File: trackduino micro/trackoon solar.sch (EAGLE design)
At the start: 53 parts, among them IC1 MCP73871, IC2 74AHC1G125DBV, SW1 SPST_TACT-KMR2, U1 ATMEGA168MLF, Y1 16MHZ

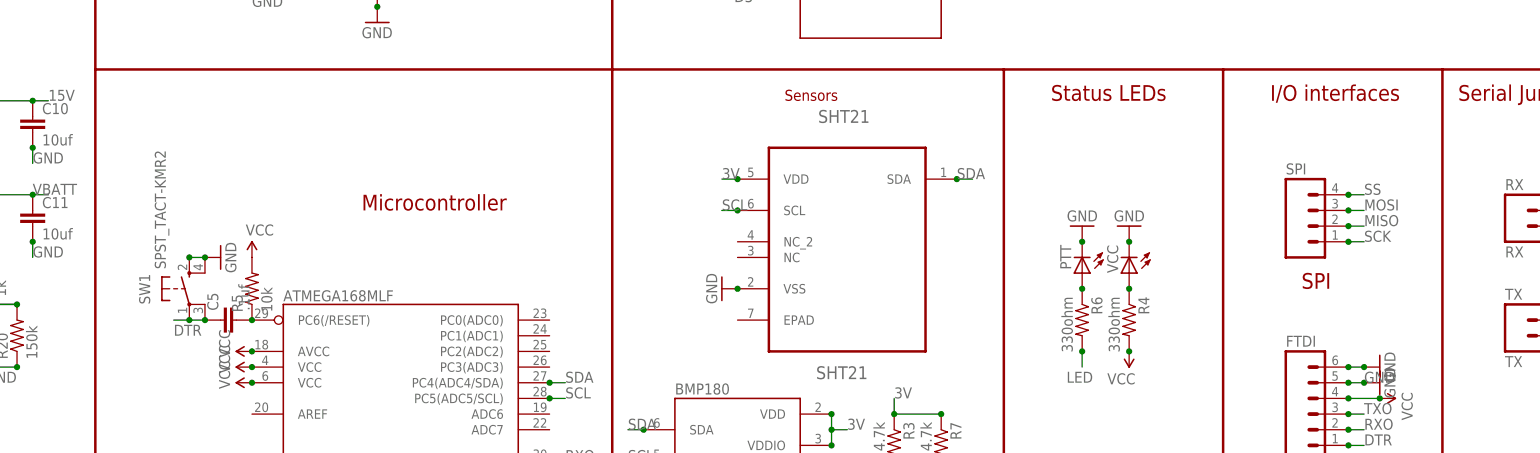
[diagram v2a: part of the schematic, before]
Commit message: added i2c breakout and fixed ftdi
added breakouts on all versions for i2c next to the spi header, replaced
IO breakout headers from .1" to 2mm to accomodate i2c.
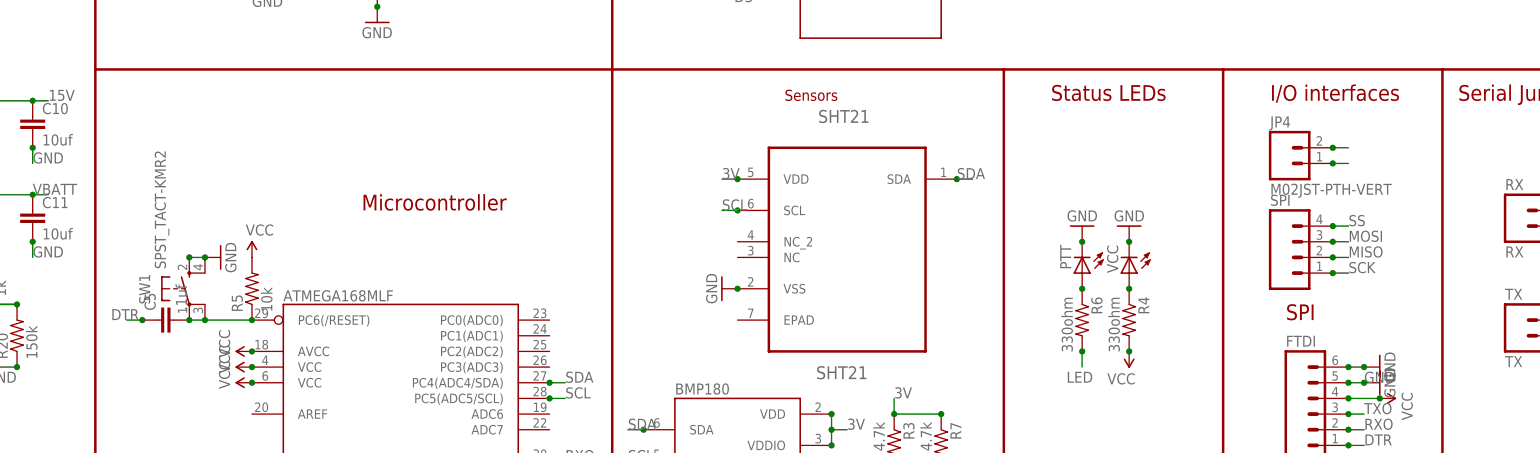
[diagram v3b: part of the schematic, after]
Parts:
- added JP4: M02JST-PTH-VERT, SparkFun-Connectors:M02JST-PTH-VERT
- SPI: device SparkFun-Connectors:M041X04_NO_SILK -> SparkFun-Connectors:M04JST-PTH-VERT
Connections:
- removed net N$7: C5.2, R5.1, U1.PC6(/RESET)
- new net N$19: C5.2, R5.1, SW1.P, SW1.P1, U1.PC6(/RESET)
- net DTR: no longer SW1.P, SW1.P1
- net SCL: now also JP4.1
- net SDA: now also JP4.2
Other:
- moved on the sheet: C5, SPI
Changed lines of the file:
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@@
 <part name="C5" library="SparkFun-Capacitors" deviceset="CAP" device="0805" value=".1uf"/>
 <part name="TX" library="SparkFun-Connectors" deviceset="M02" device="PTH" value="TX"/>
-<part name="SPI" library="SparkFun-Connectors" deviceset="M04" device="1X04_NO_SILK"/>
+<part name="SPI" library="SparkFun-Connectors" deviceset="M04" device="JST-PTH-VERT"/>
 <part name="GND23" library="SparkFun-Aesthetics" deviceset="GND" device=""/>
 <part name="FRAME1" library="SparkFun-Aesthetics" deviceset="FRAME-LETTER" device=""/>
@@
 <part name="C12" library="adafruit" deviceset="CPOL-US" device="153CLV-1012"/>
 <part name="U$3" library="SparkFun-RF" deviceset="ANTENNA2" device="SMD3"/>
+<part name="JP4" library="SparkFun-Connectors" deviceset="M02" device="JST-PTH-VERT"/>
 </parts>
 <sheets>
@@
 <text x="190.5" y="104.14" size="2.54" layer="94">I/O interfaces</text>
 <text x="220.98" y="104.14" size="2.54" layer="94">Serial Jumpers</text>
-<text x="195.58" y="73.66" size="2.54" layer="94">SPI</text>
+<text x="193.04" y="68.58" size="2.54" layer="94">SPI</text>
 <text x="195.58" y="40.64" size="2.54" layer="94">FTDI</text>
 <wire x1="147.32" y1="35.56" x2="83.82" y2="35.56" width="0.1524" layer="94"/>
@@
 <instance part="R5" gate="G$1" x="25.4" y="73.66" rot="R90"/>
 <instance part="SUPPLY10" gate="G$1" x="25.4" y="78.74"/>
-<instance part="C5" gate="G$1" x="22.86" y="68.58" rot="R90"/>
+<instance part="C5" gate="G$1" x="12.7" y="68.58" rot="R90"/>
 <instance part="TX" gate="G$1" x="231.14" y="66.04"/>
-<instance part="SPI" gate="G$1" x="198.12" y="83.82"/>
+<instance part="SPI" gate="G$1" x="195.58" y="78.74"/>
 <instance part="GND23" gate="1" x="20.32" y="78.74" rot="R90"/>
 <instance part="FRAME1" gate="G$1" x="0" y="0"/>
@@
 <instance part="C12" gate="G$1" x="-91.44" y="76.2"/>
 <instance part="U$3" gate="G$1" x="165.1" y="165.1" rot="R90"/>
+<instance part="JP4" gate="G$1" x="193.04" y="93.98"/>
 </instances>
 <busses>
@@
 </segment>
 <segment>
-<pinref part="SW1" gate="G$1" pin="P"/>
-<wire x1="15.24" y1="68.58" x2="17.78" y2="68.58" width="0.1524" layer="91"/>
-<pinref part="SW1" gate="G$1" pin="P1"/>
 <pinref part="C5" gate="G$1" pin="1"/>
-<junction x="17.78" y="68.58"/>
-<junction x="15.24" y="68.58"/>
-<wire x1="15.24" y1="68.58" x2="12.7" y2="68.58" width="0.1524" layer="91"/>
-<label x="12.7" y="66.04" size="1.778" layer="95"/>
+<wire x1="7.62" y1="68.58" x2="5.08" y2="68.58" width="0.1524" layer="91"/>
+<label x="2.54" y="68.58" size="1.778" layer="95"/>
+<junction x="7.62" y="68.58"/>
 </segment>
 </net>
@@
 <segment>
 <pinref part="SPI" gate="G$1" pin="2"/>
-<wire x1="203.2" y1="83.82" x2="205.74" y2="83.82" width="0.1524" layer="91"/>
-<label x="205.74" y="83.82" size="1.778" layer="95"/>
-<junction x="203.2" y="83.82"/>
+<wire x1="200.66" y1="78.74" x2="203.2" y2="78.74" width="0.1524" layer="91"/>
+<label x="203.2" y="78.74" size="1.778" layer="95"/>
+<junction x="200.66" y="78.74"/>
 </segment>
 </net>
@@
 <segment>
 <pinref part="SPI" gate="G$1" pin="3"/>
-<wire x1="203.2" y1="86.36" x2="205.74" y2="86.36" width="0.1524" layer="91"/>
-<label x="205.74" y="86.36" size="1.778" layer="95"/>
-<junction x="203.2" y="86.36"/>
+<wire x1="200.66" y1="81.28" x2="203.2" y2="81.28" width="0.1524" layer="91"/>
+<label x="203.2" y="81.28" size="1.778" layer="95"/>
+<junction x="200.66" y="81.28"/>
 </segment>
 </net>
@@
 <segment>
 <pinref part="SPI" gate="G$1" pin="1"/>
-<wire x1="203.2" y1="81.28" x2="205.74" y2="81.28" width="0.1524" layer="91"/>
-<label x="205.74" y="81.28" size="1.778" layer="95"/>
-<junction x="203.2" y="81.28"/>
+<wire x1="200.66" y1="76.2" x2="203.2" y2="76.2" width="0.1524" layer="91"/>
+<label x="203.2" y="76.2" size="1.778" layer="95"/>
+<junction x="200.66" y="76.2"/>
 </segment>
 </net>
@@
 <segment>
 <pinref part="SPI" gate="G$1" pin="4"/>
-<wire x1="203.2" y1="88.9" x2="205.74" y2="88.9" width="0.1524" layer="91"/>
-<label x="205.74" y="88.9" size="1.778" layer="95"/>
-<junction x="203.2" y="88.9"/>
+<wire x1="200.66" y1="83.82" x2="203.2" y2="83.82" width="0.1524" layer="91"/>
+<label x="203.2" y="83.82" size="1.778" layer="95"/>
+<junction x="200.66" y="83.82"/>
 </segment>
 </net>
@@
 <junction x="129.54" y="43.18"/>
 </segment>
+<segment>
+<pinref part="JP4" gate="G$1" pin="2"/>
+<wire x1="200.66" y1="96.52" x2="203.2" y2="96.52" width="0.1524" layer="91"/>
+<junction x="200.66" y="96.52"/>
+</segment>
 </net>
 <net name="SCL" class="0">
@@
 <label x="137.16" y="40.64" size="1.778" layer="95"/>
 <junction x="137.16" y="43.18"/>
+</segment>
+<segment>
+<pinref part="JP4" gate="G$1" pin="1"/>
+<wire x1="200.66" y1="93.98" x2="203.2" y2="93.98" width="0.1524" layer="91"/>
+<junction x="200.66" y="93.98"/>
 </segment>
 </net>
@@
 <junction x="-10.16" y="104.14"/>
 <label x="-7.62" y="104.14" size="1.778" layer="95"/>
-</segment>
-</net>
-<net name="N$7" class="0">
-<segment>
-<pinref part="U1" gate="G$1" pin="PC6(/RESET)"/>
-<pinref part="R5" gate="G$1" pin="1"/>
-<pinref part="C5" gate="G$1" pin="2"/>
-<junction x="25.4" y="68.58"/>
-<pinref part="C5" gate="G$1" pin="2"/>
 </segment>
 </net>
@@
 </segment>
 </net>
+<net name="N$19" class="0">
+<segment>
+<pinref part="C5" gate="G$1" pin="2"/>
+<pinref part="C5" gate="G$1" pin="2"/>
+<pinref part="SW1" gate="G$1" pin="P1"/>
+<wire x1="15.24" y1="68.58" x2="17.78" y2="68.58" width="0.1524" layer="91"/>
+<pinref part="U1" gate="G$1" pin="PC6(/RESET)"/>
+<pinref part="R5" gate="G$1" pin="1"/>
+<wire x1="17.78" y1="68.58" x2="25.4" y2="68.58" width="0.1524" layer="91"/>
+<junction x="25.4" y="68.58"/>
+<junction x="17.78" y="68.58"/>
+<pinref part="SW1" gate="G$1" pin="P"/>
+<junction x="15.24" y="68.58"/>
+</segment>
+</net>
